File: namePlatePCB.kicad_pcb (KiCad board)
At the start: 2 copper layers, 91 x 55 mm, 2 parts

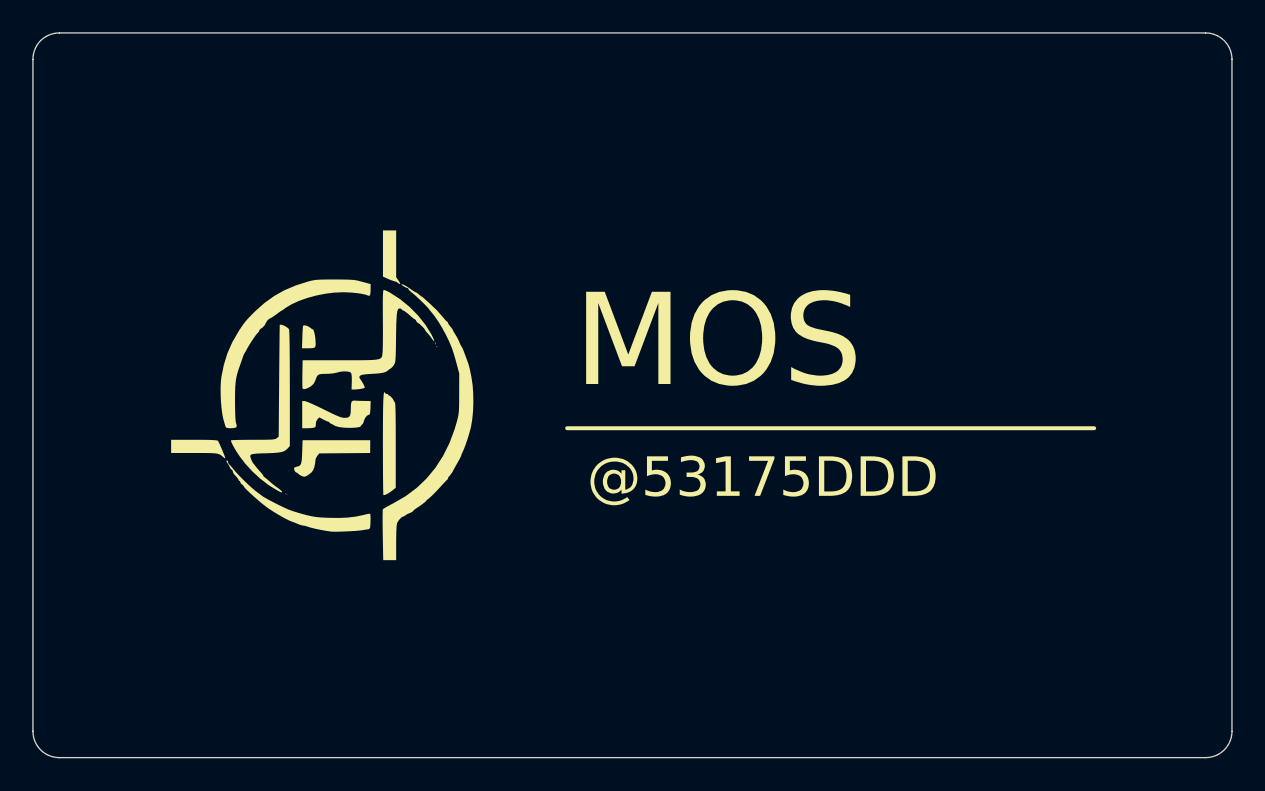
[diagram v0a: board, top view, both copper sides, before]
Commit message: ベタ追加
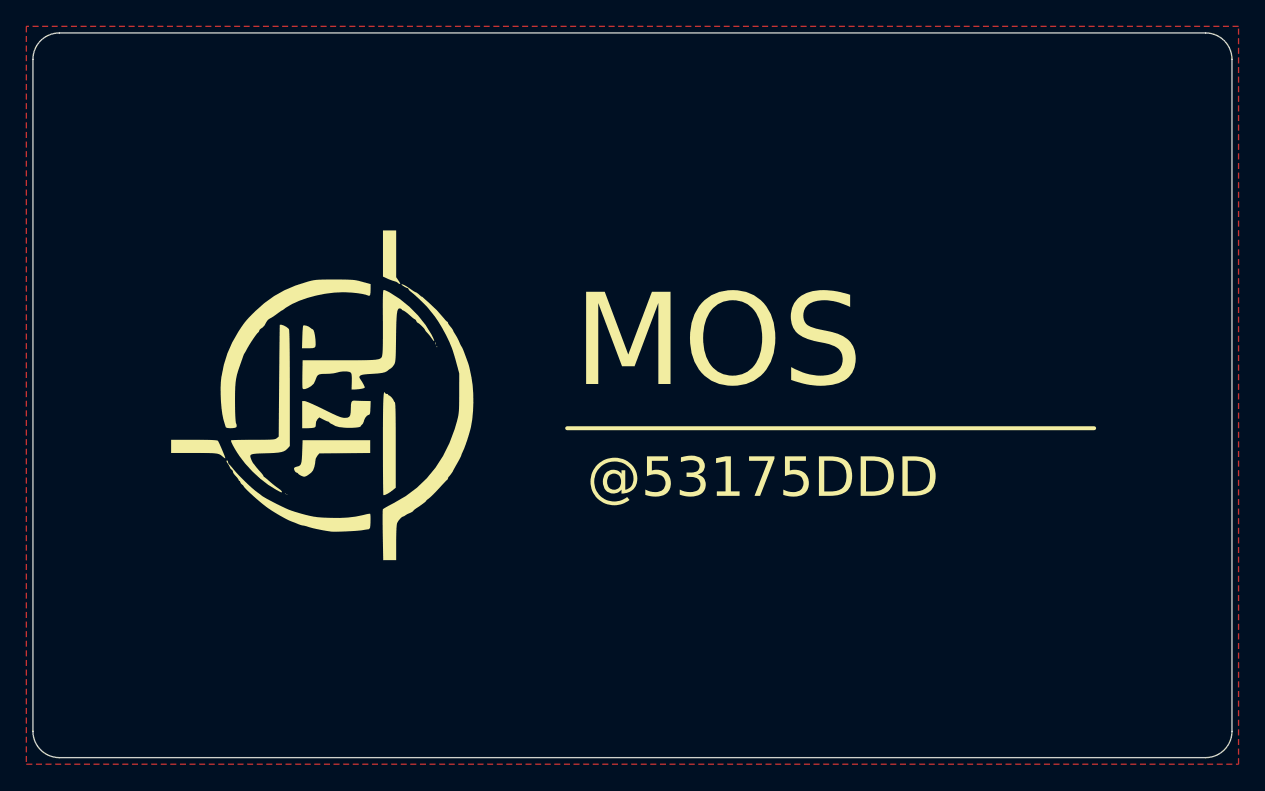
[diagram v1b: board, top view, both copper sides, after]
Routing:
- added copper zone on F.Cu, net (none)
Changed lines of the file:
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@@
     (style (thickness 0.2) (arrow_length 1.27) (text_position_mode 0) (extension_height 0.58642) (extension_offset 0.5) keep_text_aligned)
   )
+  (zone (net 0) (net_name "") (layer "F.Cu") (hatch edge 0.5)
+    (connect_pads (clearance 0.5))
+    (min_thickness 0.25) (filled_areas_thickness no)
+    (fill yes (thermal_gap 0.5) (thermal_bridge_width 0.5) (island_removal_mode 1) (island_area_min 10))
+    (polygon
+      (pts
+        (xy 191 47)
+        (xy 99 47)
+        (xy 99 103)
+        (xy 191 103)
+      )
+    )
+  )
 )
